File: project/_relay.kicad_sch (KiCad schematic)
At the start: 4 parts, among them K201 P6D-04P, Q201 AO3400A

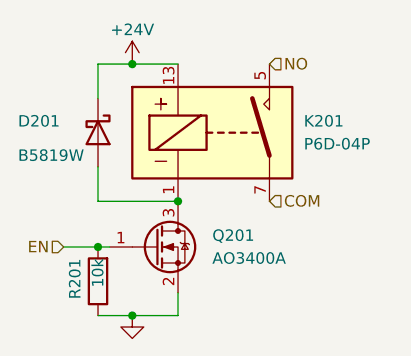
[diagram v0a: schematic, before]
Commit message: removing fets as driving is upstairs now
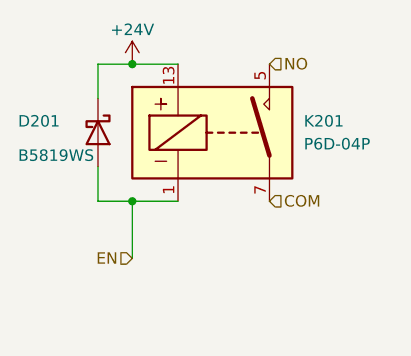
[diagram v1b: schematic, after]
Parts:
- removed Q201: AO3400A, Package_TO_SOT_SMD:SOT-23, symbol Transistor_FET:AO3400A
- removed R201: 10k, Resistor_SMD:R_0805_2012Metric, symbol Device:R
- D201: value B5819W -> B5819WS; footprint Diode_SMD:D_SOD-123 -> Diode_SMD:D_SOD-323_HandSoldering; jlc-part-type B -> E; lcsc# C8598 -> C402231
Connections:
- net EN: now also D201.2 (A), K201.1
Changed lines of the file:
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@@
     (company "makerspace.lt")
-  )
-  (junction (at 135.89 114.3) (diameter 0) (color 0 0 0 0)
-  )
-  (junction (at 127 119.38) (diameter 0) (color 0 0 0 0)
   )
   (junction (at 130.81 99.06) (diameter 0) (color 0 0 0 0)
   )
-  (junction (at 130.81 127) (diameter 0) (color 0 0 0 0)
-  )
-  (wire (pts (xy 130.81 127) (xy 135.89 127))
-    (stroke (width 0) (type default) (color 0 0 0 0))
+  (junction (at 130.81 114.3) (diameter 0) (color 0 0 0 0)
   )
   (wire (pts (xy 130.81 99.06) (xy 135.89 99.06))
     (stroke (width 0) (type default) (color 0 0 0 0))
   )
-  (wire (pts (xy 123.19 119.38) (xy 127 119.38))
+  (wire (pts (xy 130.81 114.3) (xy 135.89 114.3))
     (stroke (width 0) (type default) (color 0 0 0 0))
   )
@@
     (stroke (width 0) (type default) (color 0 0 0 0))
   )
-  (wire (pts (xy 127 127) (xy 130.81 127))
-    (stroke (width 0) (type default) (color 0 0 0 0))
-  )
-  (wire (pts (xy 127 119.38) (xy 128.27 119.38))
-    (stroke (width 0) (type default) (color 0 0 0 0))
-  )
-  (wire (pts (xy 135.89 127) (xy 135.89 124.46))
-    (stroke (width 0) (type default) (color 0 0 0 0))
-  )
   (wire (pts (xy 127 99.06) (xy 130.81 99.06))
     (stroke (width 0) (type default) (color 0 0 0 0))
   )
-  (wire (pts (xy 127 114.3) (xy 135.89 114.3))
+  (wire (pts (xy 127 114.3) (xy 130.81 114.3))
+    (stroke (width 0) (type default) (color 0 0 0 0))
+  )
+  (wire (pts (xy 130.81 114.3) (xy 130.81 120.65))
     (stroke (width 0) (type default) (color 0 0 0 0))
   )
@@
     (effects (font (size 1.27 1.27)) (justify left))
   )
-  (hierarchical_label "EN" (shape input) (at 123.19 119.38 180)
+  (hierarchical_label "EN" (shape input) (at 130.81 120.65 180)
     (effects (font (size 1.27 1.27)) (justify right))
   )
@@
       (effects (font (size 1.27 1.27)) (justify left))
     )
-    (property "Value" "B5819W" (id 1) (at 118.11 109.22 90)
+    (property "Value" "B5819WS" (id 1) (at 118.11 109.22 90)
       (effects (font (size 1.27 1.27)) (justify left))
     )
-    (property "Footprint" "Diode_SMD:D_SOD-123" (id 2) (at 127 106.68 0)
+    (property "Footprint" "Diode_SMD:D_SOD-323_HandSoldering" (id 2) (at 127 106.68 0)
       (effects (font (size 1.27 1.27)) hide)
     )
-    (property "Datasheet" "~" (id 3) (at 127 106.68 0)
+    (property "Datasheet" "https://www.lcsc.com/datasheet/lcsc_datasheet_1912111437_LGE-B5819WS_C402231.pdf" (id 3) (at 127 106.68 0)
       (effects (font (size 1.27 1.27)) hide)
     )
-    (property "jlc-part-type" "B" (id 4) (at 127 106.68 0)
+    (property "jlc-part-type" "E" (id 4) (at 127 106.68 0)
       (effects (font (size 1.27 1.27)) hide)
     )
-    (property "lcsc#" "C8598" (id 5) (at 127 106.68 0)
+    (property "lcsc#" "C402231" (id 5) (at 127 106.68 0)
       (effects (font (size 1.27 1.27)) hide)
     )
@@
     (pin "7")
   )
-  (symbol (lib_id "-pwr:GND") (at 130.81 127 0) (unit 1)
-    (in_bom yes) (on_board yes) (fields_autoplaced)
-    (property "Reference" "#PWR0202" (id 0) (at 130.81 133.35 0)
-      (effects (font (size 1.27 1.27)) hide)
-    )
-    (property "Value" "GND" (id 1) (at 130.81 130.81 0)
-      (effects (font (size 1.27 1.27)) hide)
-    )
-    (property "Footprint" "" (id 2) (at 130.81 127 0)
-      (effects (font (size 1.27 1.27)) hide)
-    )
-    (property "Datasheet" "" (id 3) (at 130.81 127 0)
-      (effects (font (size 1.27 1.27)) hide)
-    )
-    (pin "1")
-  )
-  (symbol (lib_id "Transistor_FET:AO3400A") (at 133.35 119.38 0) (unit 1)
-    (in_bom yes) (on_board yes) (fields_autoplaced)
-    (property "Reference" "Q201" (id 0) (at 139.7 118.1099 0)
-      (effects (font (size 1.27 1.27)) (justify left))
-    )
-    (property "Value" "AO3400A" (id 1) (at 139.7 120.6499 0)
-      (effects (font (size 1.27 1.27)) (justify left))
-    )
-    (property "Footprint" "Package_TO_SOT_SMD:SOT-23" (id 2) (at 138.43 121.285 0)
-      (effects (font (size 1.27 1.27) italic) (justify left) hide)
-    )
-    (property "Datasheet" "http://www.aosmd.com/pdfs/datasheet/AO3400A.pdf" (id 3) (at 133.35 119.38 0)
-      (effects (font (size 1.27 1.27)) (justify left) hide)
-    )
-    (property "jlc-part-type" "B" (id 4) (at 133.35 119.38 0)
-      (effects (font (size 1.27 1.27)) hide)
-    )
-    (property "lcsc#" "C20917" (id 5) (at 133.35 119.38 0)
-      (effects (font (size 1.27 1.27)) hide)
-    )
-    (pin "1")
-    (pin "2")
-    (pin "3")
-  )
   (symbol (lib_id "power:+24V") (at 130.81 99.06 0) (unit 1)
     (in_bom no) (on_board no)
@@
     (pin "1")
   )
-  (symbol (lib_id "Device:R") (at 127 123.19 180) (unit 1)
-    (in_bom yes) (on_board yes)
-    (property "Reference" "R201" (id 0) (at 124.46 120.65 90)
-      (effects (font (size 1.27 1.27)) (justify left))
-    )
-    (property "Value" "10k" (id 1) (at 127 120.65 90)
-      (effects (font (size 1.27 1.27)) (justify left))
-    )
-    (property "Footprint" "Resistor_SMD:R_0805_2012Metric" (id 2) (at 128.778 123.19 90)
-      (effects (font (size 1.27 1.27)) hide)
-    )
-    (property "Datasheet" "~" (id 3) (at 127 123.19 0)
-      (effects (font (size 1.27 1.27)) hide)
-    )
-    (property "jlc-part-type" "B" (id 4) (at 127 123.19 0)
-      (effects (font (size 1.27 1.27)) hide)
-    )
-    (property "lcsc#" "C17414" (id 5) (at 127 123.19 0)
-      (effects (font (size 1.27 1.27)) hide)
-    )
-    (pin "1")
-    (pin "2")
-  )
 )
